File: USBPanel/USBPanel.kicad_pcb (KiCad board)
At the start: 6 copper layers, 36 x 38 mm, 68 parts, among them J1 PORT1, J2 PORT2, J3 PWR, J4 USB_UFP, J5 SINK, J6 I2Ct, J7 I2Cc, Q1 ISZ0702NLS, Q2 ISZ0702NLS, Q3 NX138BK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

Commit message: USBPanel PCB complete
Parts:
- added C18: 10μF 50V, Capacitor_SMD:C_1206_3216Metric, B.Cu at (147.5, 103.6)
- moved R17 6.58 mm to (163.2, 104.6), turned to -90 degrees
- moved R15 6.30 mm to (164.8, 104.6), turned to -90 degrees
- moved R16 5.77 mm to (161.6, 105.3), turned to -90 degrees
- moved TP3 4.92 mm to (155.4, 82.7), turned to -90 degrees
- moved TP2 1.84 mm to (143.2, 115.7)
- moved REF** 1.14 mm to (162.2, 113.9)
- moved TP6 1.14 mm to (146.0, 104.1)
- moved C9 0.95 mm to (144.4, 95.0)
- moved U1 0.70 mm to (140.1, 96.0)
- moved R3 0.50 mm to (142.7, 98.8)
- moved C10 0.42 mm to (144.4, 93.4)
- moved C1 0.40 mm to (138.1, 92.9)
- moved C2 0.40 mm to (138.1, 95.0)
- moved C3 0.40 mm to (138.1, 97.1)
- moved Q1 0.30 mm to (145.8, 98.3)
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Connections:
- net Net-(D1-A1) renamed /PORT2_VBUS
- net Net-(Q1-S) renamed /PORT1_VBUS
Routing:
- net +3.3V: track 0.00 -> 95.6 mm, vias 0 -> 4
- net GND: track 1.21 -> 54.1 mm, vias 0 -> 55
- net /PORT1_UFP: track 0.00 -> 48.8 mm, vias 0 -> 2
- net /PORT2_EN: track 0.00 -> 28.9 mm, vias 0 -> 3
- net /PORT2_VBUS: track 6.67 -> 33.7 mm, vias 6 -> 14
- net Net-(Q4-G): track 0.00 -> 24.8 mm, vias 0 -> 1
- net Net-(U4-~{FAULT}): track 0.00 -> 22.5 mm, vias 0 -> 1
- net +5V: track 0.00 -> 19.4 mm, vias 0 -> 24
- net Net-(U4-~{LD_DET}): track 0.00 -> 19.1 mm, vias 0 -> 1
- net /PORT1_VBUS: track 6.58 -> 25.1 mm, vias 6 -> 21
- net Net-(U4-~{UFP}): track 0.00 -> 16.7 mm, vias 0 -> 1
- net Net-(J5-Pin_1): track 0.00 -> 16.6 mm, vias 0 -> 1
- net Net-(Q4-D): track 0.00 -> 14.7 mm
- net /PORT1_D+: track 2.84 -> 17.2 mm
- net Net-(J2-CC1): track 0.00 -> 14.2 mm, vias 0 -> 1
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- added copper zone on In2.Cu, net /PORT1_VBUS
- added copper zone on In3.Cu, net /PORT1_VBUS
- added copper zone on In2.Cu, net /PORT2_VBUS
- added copper zone on In3.Cu, net /PORT2_VBUS
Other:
- outline, holes or cut-outs redrawn
- board text added: "+OUT-"
- board text added: "5V 3.3V GND"
- board text added: "5V: Max 3.6A"
- board text added: "I2Cc"
- board text added: "I2Ct"
- board text added: "Modular Audio USB Panel 5V 3A"
- board text added: "Port 1 5V 3A USB 2.0"
- board text added: "Port 1 Data"
- board text added: "Port 2 5V 3A No Data Off if P1 active"
- board text added: "WP"

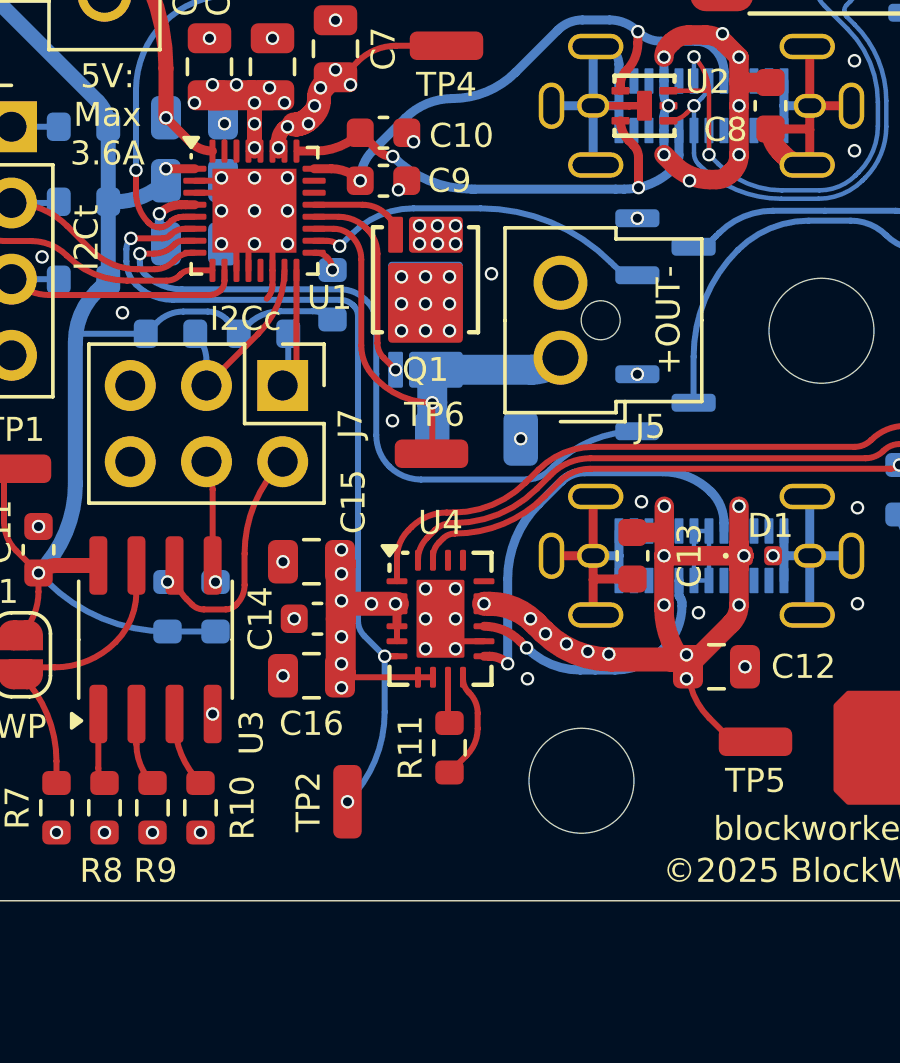
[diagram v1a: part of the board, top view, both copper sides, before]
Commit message: USBPanel and I/O panel stuff ordered
Includes small changes and fixes for the USBPanel PCB, the main panel design itself, and various small parts for it
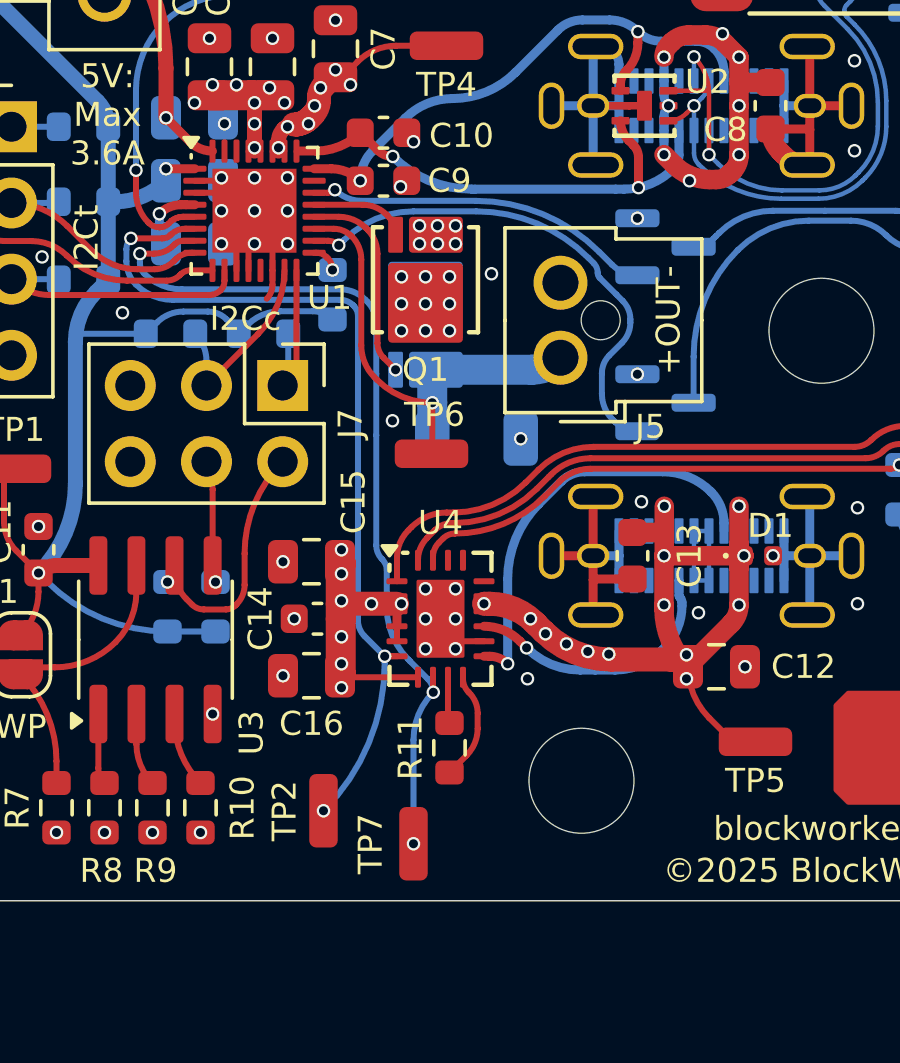
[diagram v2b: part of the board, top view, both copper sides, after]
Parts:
- added TP7: PORT2_HI, BW_PassiveMechanical:TP_0603_1608Metric_Fused, F.Cu at (145.4, 117.1)
- D2, D3: footprint LED_SMD:LED_Cree-PLCC4_2x2mm_CW -> BW_Active:LED_Cree-PLCC4_2x2mm_CW
- moved TP2 0.85 mm to (142.4, 116.0)
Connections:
- U1 pad 18: Net-(Q5-G) -> Net-(Q4-G)
- U1 pad 22: unconnected-(U1-GPIO4-Pad22) -> Net-(Q5-G)
- U1 pad 7: Net-(Q4-G) -> /PORT2_HI
- U4 pad 8: +5V -> /PORT2_HI
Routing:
- net /PORT2_HI: track 0.00 -> 29.4 mm, vias 0 -> 3
- net Net-(Q4-G): track 24.8 -> 17.1 mm
- net /PORT2_EN: track 28.9 -> 29.4 mm
- net +5V: track 19.4 -> 18.9 mm
